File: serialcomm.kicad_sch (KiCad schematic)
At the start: 5 parts, among them J2 USB_B_Micro, U17 W65C51NxP, U19 FT232RL, X4 1.8432 MHz

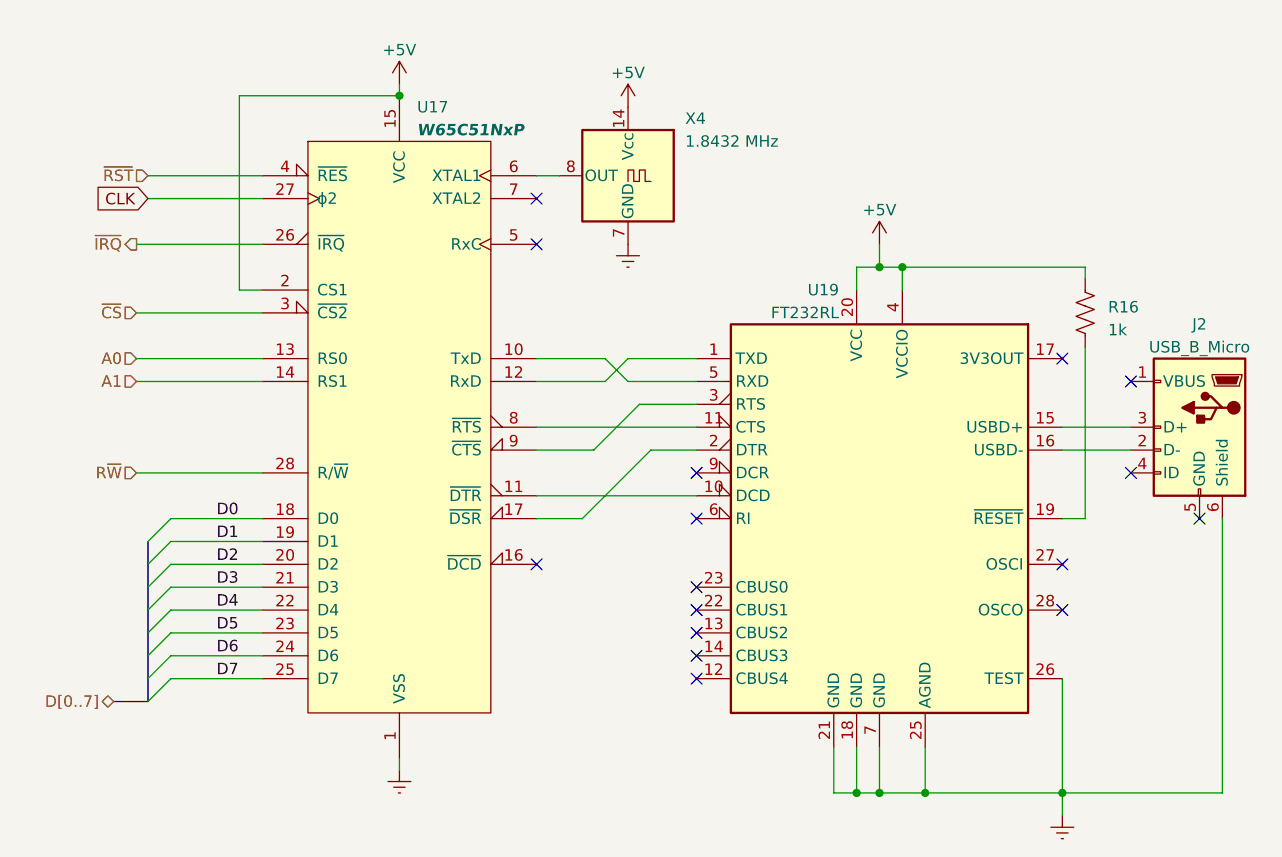
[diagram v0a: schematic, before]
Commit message: RS-232/ACIA works!
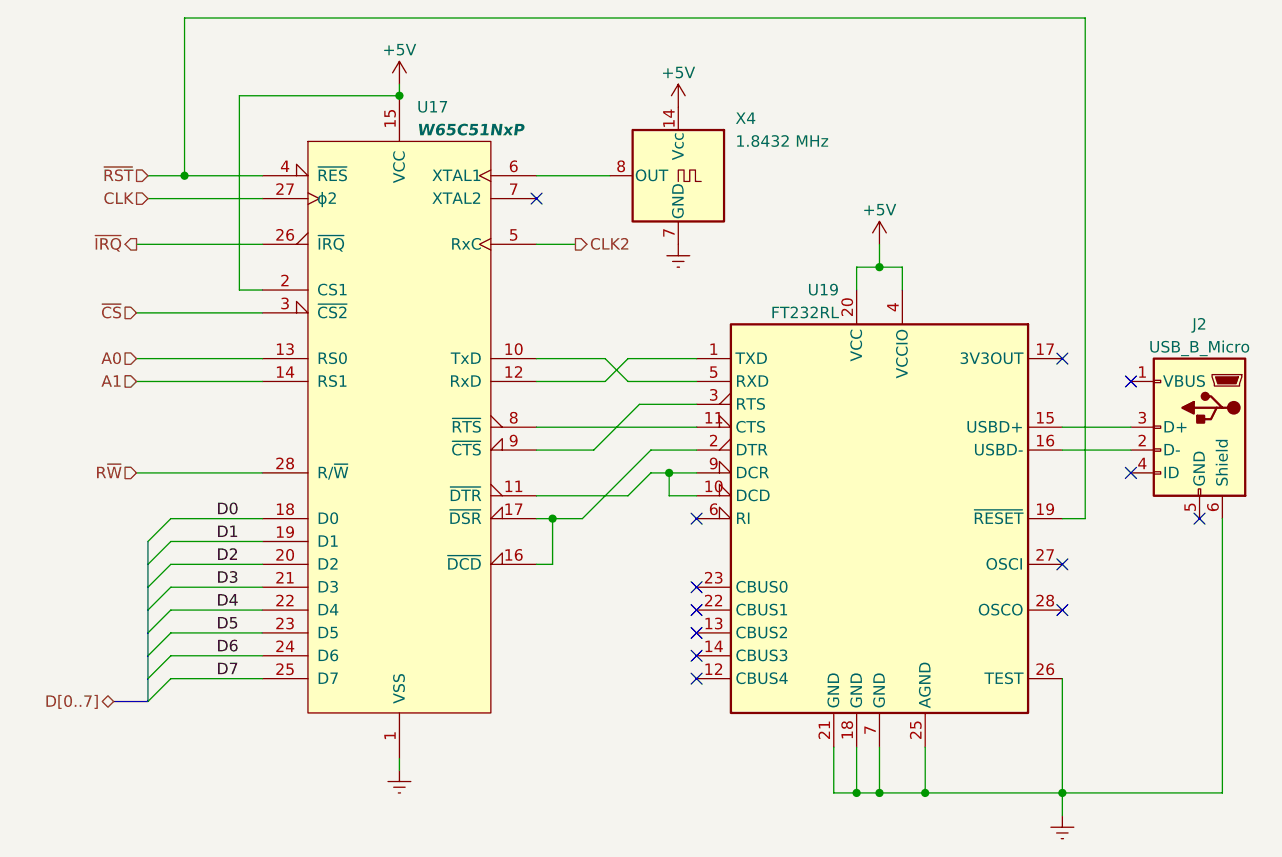
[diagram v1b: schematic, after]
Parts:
- removed R16: 1k, symbol Device:R_US
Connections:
- net ~{RST}: now also U19.19 (~{RESET})
- net at U17.11 (~{DTR}), U19.10 (DCD): now also U19.9 (DCR)
- net at U17.16 (~{DCD}): now also U17.17 (~{DSR}), U19.2 (DTR)
- net CLK2: now reaches U17.5 (RxC)
- no-connect marks 16 -> 13
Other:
- moved on the sheet: X4
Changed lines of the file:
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@@
   (junction (at 119.38 106.68) (diameter 0) (color 0 0 0 0)
   )
+  (junction (at 77.978 76.2) (diameter 0) (color 0 0 0 0)
+  )
+  (junction (at 90.932 71.12) (diameter 0) (color 0 0 0 0)
+  )
   (junction (at 134.62 106.68) (diameter 0) (color 0 0 0 0)
   )
-  (junction (at 116.84 48.26) (diameter 0) (color 0 0 0 0)
+  (junction (at 37.084 38.1) (diameter 0) (color 0 0 0 0)
   )
   (junction (at 114.3 106.68) (diameter 0) (color 0 0 0 0)
@@
   (no_connect (at 93.98 88.9))
   (no_connect (at 134.62 81.28))
-  (no_connect (at 93.98 71.12))
   (no_connect (at 93.98 93.98))
-  (no_connect (at 76.2 81.28))
   (no_connect (at 76.2 40.64))
   (no_connect (at 134.62 58.42))
-  (no_connect (at 76.2 45.72))
   (no_connect (at 149.86 76.2))
   (no_connect (at 93.98 91.44))
@@
     (stroke (width 0) (type default))
   )
+  (wire (pts (xy 37.084 38.1) (xy 33.02 38.1))
+    (stroke (width 0) (type default))
+  )
   (wire (pts (xy 35.56 86.36) (xy 45.72 86.36))
     (stroke (width 0) (type default))
@@
     (stroke (width 0) (type default))
   )
+  (wire (pts (xy 88.9 71.12) (xy 90.932 71.12))
+    (stroke (width 0) (type default))
+  )
   (wire (pts (xy 114.3 101.6) (xy 114.3 106.68))
     (stroke (width 0) (type default))
@@
     (stroke (width 0) (type default))
   )
-  (wire (pts (xy 76.2 38.1) (xy 78.74 38.1))
-    (stroke (width 0) (type default))
-  )
   (bus (pts (xy 33.02 88.9) (xy 33.02 91.44))
     (stroke (width 0) (type default))
@@
     (stroke (width 0) (type default))
   )
+  (wire (pts (xy 93.98 73.66) (xy 90.932 73.66))
+    (stroke (width 0) (type default))
+  )
   (wire (pts (xy 35.56 88.9) (xy 45.72 88.9))
     (stroke (width 0) (type default))
@@
     (stroke (width 0) (type default))
   )
-  (wire (pts (xy 137.16 48.26) (xy 137.16 49.53))
-    (stroke (width 0) (type default))
-  )
   (wire (pts (xy 31.75 71.12) (xy 45.72 71.12))
     (stroke (width 0) (type default))
@@
     (stroke (width 0) (type default))
   )
+  (wire (pts (xy 90.932 71.12) (xy 93.98 71.12))
+    (stroke (width 0) (type default))
+  )
   (wire (pts (xy 31.75 60.96) (xy 45.72 60.96))
     (stroke (width 0) (type default))
   )
+  (wire (pts (xy 86.36 73.66) (xy 88.9 71.12))
+    (stroke (width 0) (type default))
+  )
   (wire (pts (xy 35.56 76.2) (xy 45.72 76.2))
     (stroke (width 0) (type default))
   )
-  (wire (pts (xy 45.72 38.1) (xy 33.02 38.1))
-    (stroke (width 0) (type default))
-  )
-  (wire (pts (xy 116.84 48.26) (xy 137.16 48.26))
+  (wire (pts (xy 45.72 38.1) (xy 37.084 38.1))
+    (stroke (width 0) (type default))
+  )
+  (wire (pts (xy 76.2 45.72) (xy 80.518 45.72))
     (stroke (width 0) (type default))
   )
@@
     (stroke (width 0) (type default))
   )
+  (wire (pts (xy 137.16 20.574) (xy 37.084 20.574))
+    (stroke (width 0) (type default))
+  )
   (wire (pts (xy 152.4 76.2) (xy 152.4 106.68))
     (stroke (width 0) (type default))
@@
     (stroke (width 0) (type default))
   )
+  (wire (pts (xy 76.2 38.1) (xy 84.328 38.1))
+    (stroke (width 0) (type default))
+  )
   (wire (pts (xy 35.56 78.74) (xy 45.72 78.74))
     (stroke (width 0) (type default))
@@
     (stroke (width 0) (type default))
   )
+  (wire (pts (xy 37.084 20.574) (xy 37.084 38.1))
+    (stroke (width 0) (type default))
+  )
+  (wire (pts (xy 90.932 73.66) (xy 90.932 71.12))
+    (stroke (width 0) (type default))
+  )
   (bus (pts (xy 33.02 83.82) (xy 33.02 86.36))
     (stroke (width 0) (type default))
   )
+  (wire (pts (xy 77.978 81.28) (xy 77.978 76.2))
+    (stroke (width 0) (type default))
+  )
+  (wire (pts (xy 77.978 76.2) (xy 81.28 76.2))
+    (stroke (width 0) (type default))
+  )
+  (wire (pts (xy 76.2 73.66) (xy 86.36 73.66))
+    (stroke (width 0) (type default))
+  )
   (wire (pts (xy 82.55 68.58) (xy 87.63 63.5))
     (stroke (width 0) (type default))
@@
     (stroke (width 0) (type default))
   )
-  (wire (pts (xy 76.2 73.66) (xy 93.98 73.66))
+  (wire (pts (xy 76.2 81.28) (xy 77.978 81.28))
     (stroke (width 0) (type default))
   )
@@
     (stroke (width 0) (type default))
   )
-  (wire (pts (xy 137.16 76.2) (xy 137.16 57.15))
-    (stroke (width 0) (type default))
-  )
-  (wire (pts (xy 76.2 76.2) (xy 81.28 76.2))
+  (wire (pts (xy 137.16 20.574) (xy 137.16 76.2))
+    (stroke (width 0) (type default))
+  )
+  (wire (pts (xy 76.2 76.2) (xy 77.978 76.2))
     (stroke (width 0) (type default))
   )
@@
     (effects (font (size 1.27 1.27)) (justify left bottom))
   )
-  (global_label "CLK" (shape input) (at 33.02 40.64 180) (fields_autoplaced)
-    (effects (font (size 1.27 1.27)) (justify right))
-    (property "Intersheetrefs" "${INTERSHEET_REFS}" (at 26.5461 40.64 0)
-      (effects (font (size 1.27 1.27)) (justify right) hide)
-    )
-  )
   (hierarchical_label "R~{W}" (shape input) (at 31.75 71.12 180) (fields_autoplaced)
     (effects (font (size 1.27 1.27)) (justify right))
@@
   (hierarchical_label "A1" (shape input) (at 31.75 60.96 180) (fields_autoplaced)
     (effects (font (size 1.27 1.27)) (justify right))
+  )
+  (hierarchical_label "CLK2" (shape output) (at 80.518 45.72 0) (fields_autoplaced)
+    (effects (font (size 1.27 1.27)) (justify left))
   )
   (hierarchical_label "~{CS}" (shape input) (at 31.75 53.34 180) (fields_autoplaced)
@@
   )
   (hierarchical_label "~{RST}" (shape input) (at 33.02 38.1 180) (fields_autoplaced)
+    (effects (font (size 1.27 1.27)) (justify right))
+  )
+  (hierarchical_label "CLK" (shape input) (at 33.02 40.64 180) (fields_autoplaced)
     (effects (font (size 1.27 1.27)) (justify right))
   )
@@
     )
   )
-  (symbol (lib_id "power:VCC") (at 86.36 30.48 0) (unit 1)
+  (symbol (lib_id "power:VCC") (at 91.948 30.48 0) (unit 1)
     (in_bom yes) (on_board yes) (dnp no) (fields_autoplaced)
-    (property "Reference" "#PWR025" (at 86.36 34.29 0)
-      (effects (font (size 1.27 1.27)) hide)
-    )
-    (property "Value" "+5V" (at 86.36 26.67 0)
+    (property "Reference" "#PWR025" (at 91.948 34.29 0)
+      (effects (font (size 1.27 1.27)) hide)
+    )
+    (property "Value" "+5V" (at 91.948 26.67 0)
       (effects (font (size 1.27 1.27)))
     )
-    (property "Footprint" "" (at 86.36 30.48 0)
-      (effects (font (size 1.27 1.27)) hide)
-    )
-    (property "Datasheet" "" (at 86.36 30.48 0)
+    (property "Footprint" "" (at 91.948 30.48 0)
+      (effects (font (size 1.27 1.27)) hide)
+    )
+    (property "Datasheet" "" (at 91.948 30.48 0)
       (effects (font (size 1.27 1.27)) hide)
     )
@@
     )
   )
-  (symbol (lib_id "power:Earth") (at 86.36 45.72 0) (unit 1)
+  (symbol (lib_id "power:Earth") (at 91.948 45.72 0) (unit 1)
     (in_bom yes) (on_board yes) (dnp no) (fields_autoplaced)
-    (property "Reference" "#PWR026" (at 86.36 52.07 0)
-      (effects (font (size 1.27 1.27)) hide)
-    )
-    (property "Value" "Earth" (at 86.36 49.53 0)
-      (effects (font (size 1.27 1.27)) hide)
-    )
-    (property "Footprint" "" (at 86.36 45.72 0)
-      (effects (font (size 1.27 1.27)) hide)
-    )
-    (property "Datasheet" "~" (at 86.36 45.72 0)
+    (property "Reference" "#PWR026" (at 91.948 52.07 0)
+      (effects (font (size 1.27 1.27)) hide)
+    )
+    (property "Value" "Earth" (at 91.948 49.53 0)
+      (effects (font (size 1.27 1.27)) hide)
+    )
+    (property "Footprint" "" (at 91.948 45.72 0)
+      (effects (font (size 1.27 1.27)) hide)
+    )
+    (property "Datasheet" "~" (at 91.948 45.72 0)
       (effects (font (size 1.27 1.27)) hide)
     )
@@
         (path "/031ea57b-8d17-4b45-87cc-c58302485ce1/c43edb08-6809-4421-aa3d-4af594c68b1c"
           (reference "#PWR028") (unit 1)
-        )
-      )
-    )
-  )
-  (symbol (lib_id "Device:R_US") (at 137.16 53.34 0) (unit 1)
-    (in_bom yes) (on_board yes) (dnp no)
-    (property "Reference" "R16" (at 139.7 52.705 0)
-      (effects (font (size 1.27 1.27)) (justify left))
-    )
-    (property "Value" "1k" (at 139.7 55.245 0)
-      (effects (font (size 1.27 1.27)) (justify left))
-    )
-    (property "Footprint" "" (at 138.176 53.594 90)
-      (effects (font (size 1.27 1.27)) hide)
-    )
-    (property "Datasheet" "~" (at 137.16 53.34 0)
-      (effects (font (size 1.27 1.27)) hide)
-    )
-    (pin "1")
-    (pin "2")
-    (instances
-      (project "rod6502"
-        (path "/031ea57b-8d17-4b45-87cc-c58302485ce1"
-          (reference "R16") (unit 1)
-        )
-        (path "/031ea57b-8d17-4b45-87cc-c58302485ce1/c43edb08-6809-4421-aa3d-4af594c68b1c"
-          (reference "R2") (unit 1)
         )
       )
@@
     )
   )
-  (symbol (lib_id "Oscillator:ACO-xxxMHz") (at 86.36 38.1 0) (mirror y) (unit 1)
+  (symbol (lib_id "Oscillator:ACO-xxxMHz") (at 91.948 38.1 0) (mirror y) (unit 1)
     (in_bom yes) (on_board yes) (dnp no)
-    (property "Reference" "X4" (at 92.71 31.75 0)
+    (property "Reference" "X4" (at 98.298 31.75 0)
       (effects (font (size 1.27 1.27)) (justify right))
     )
-    (property "Value" "1.8432 MHz" (at 92.71 34.29 0)
+    (property "Value" "1.8432 MHz" (at 98.298 34.29 0)
       (effects (font (size 1.27 1.27)) (justify right))
     )
-    (property "Footprint" "Oscillator:Oscillator_DIP-14" (at 74.93 46.99 0)
-      (effects (font (size 1.27 1.27)) hide)
-    )
-    (property "Datasheet" "http://www.conwin.com/datasheets/cx/cx030.pdf" (at 88.9 38.1 0)
-      (effects (font (size 1.27 1.27)) hide)
-    )
+    (property "Footprint" "Oscillator:Oscillator_DIP-14" (at 80.518 46.99 0)
+      (effects (font (size 1.27 1.27)) hide)
+    )
+    (property "Datasheet" "http://www.conwin.com/datasheets/cx/cx030.pdf" (at 94.488 38.1 0)
+      (effects (font (size 1.27 1.27)) hide)
+    )
